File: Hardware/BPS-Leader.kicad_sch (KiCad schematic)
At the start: 27 parts, among them J17 Conn_01x04, J21 SFH11-PBPC-D05-ST-BK, J5 Conn_02x06_Counter_Clockwise, J6 PeripheralCAN, J7 PeripheralCAN, J8 CarCANConnector, Q11 PSMN8R5-40MSDX, U12 SHT4x

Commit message: revB updates
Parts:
- removed J17: Conn_01x04, UTSVT_Connectors:Molex_Nano-Fit_105309-xx04_1x04_P2.50mm_Vertical, symbol Connector_Generic:Conn_01x04
- removed J6: PeripheralCAN, UTSVT_Connectors:Molex_Nano-Fit_105309-xx04_1x04_P2.50mm_Vertical, symbol utsvt_connectors:PeripheralCANConnector
- removed LOGO2: UTSVT, UTSVT_Logos:LHRs_LOGO, symbol UTSVT_Misc:Logo_Placeholder
- removed LOGO3: Hallock, UTSVT_Logos:Hallock_Image_Small, symbol UTSVT_Misc:Logo_Placeholder
- removed Q11: PSMN8R5-40MSDX, UTSVT_Power:PSMN8R5-40MSDX, symbol Transistor_FET:BUK7M27-80EX
- added F3, F5: 3568, FUSE 3568:3568, symbol 3568:3568
- added J4: PeripheralCAN, UTSVT_Connectors:Molex_Nano-Fit_105309-xx04_1x04_P2.50mm_Vertical, symbol utsvt_connectors:PeripheralCANConnector
- added LOGO1, LOGO2, LOGO3, LOGO4: Dr. Hallock, symbol utsvt_misc:Logo_Placeholder
- added Q11: IRLML0030, Package_TO_SOT_SMD:SOT-23, symbol Transistor_FET:IRLML0030
- added R16, R17: 10k, Resistor_SMD:R_0603_1608Metric, symbol Device:R_US
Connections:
- net +24V: now also F3.2, F3.4, F5.2, F5.4; no longer J7.1 (24V)
- net +3.3V: now also R16.1, R17.1
- net ARRAY_PRE_CONTROL: now also J1.16 (SPI3_NSS); no longer J1.47 (ADC2_IN12)
- net CAR_CAN+: no longer J1.30 (CarCAN_H), J8.1 (CAN_H)
- net CAR_CAN-: no longer J1.32 (CarCAN_L), J8.2 (CAN_L)
- net ESP_RESET: now also J1.48 (SPI2_NSS); no longer J1.17 (UART5_TX)
- net FAN_ALERT: now also J1.47 (ADC2_IN12); no longer J1.31 (OPAMP5_VINM)
- net GND: now also J4.2 (GND), Q11.2 (S)
- net LED_RCLK: no longer J21.5 (CH5)
- net LED_SER: now also J1.20 (SPI3_SCK); no longer J1.16 (SPI3_NSS)
- net STROBE_CONN_24V-: now also Q11.3 (D)
- net STROBE_CONN_3.3V: now also Q11.1 (G)
- net BPS_CAN+ renamed BPS_CAN_H
- net BPS_CAN_H: now also J4.3 (CAN_H)
- net BPS_CAN- renamed BPS_CAN_L
- net BPS_CAN_L: now also J4.4 (CAN_L)
- net FAN+HTSense_SCL renamed HTSense_SCL
- net HTSense_SCL: now also J21.5 (CH5), R16.2; no longer J21.6 (CH4)
- net FAN+HTSense_SDA renamed HTSense_SDA
- net HTSense_SDA: now also J21.6 (CH4), R17.2; no longer J21.7 (CH3)
- net FAN_1_PWM renamed FAN_SDA
- net FAN_2_PWM renamed FAN_SCL
- net FAN_SCL: now also J21.7 (CH3)
- new net: F3.1, F3.3, J7.1 (24V)
- new net: F5.1, F5.3, J4.1 (24V)
- new net CAR_CAN_H: J1.30 (CarCAN_H), J8.1 (CAN_H)
- new net CAR_CAN_L: J1.32 (CarCAN_L), J8.2 (CAN_L)
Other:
- sheet Contactor Control and Sense ports: added ARRAY_PRE_VOLTAGE+_ADC, ARRAY_PRE_VOLTAGE-_ADC; removed none
- sheet Fan Controller ports: added none; removed FAN_1_PWM, FAN_2_PWM
- note added: "Icons"
- note removed: "(to be updated)"
- note removed: "Analog Input"
- note removed: "Load-bearing Icons"
- moved on the sheet: C36, J7, J8, TP2, TP3, U12

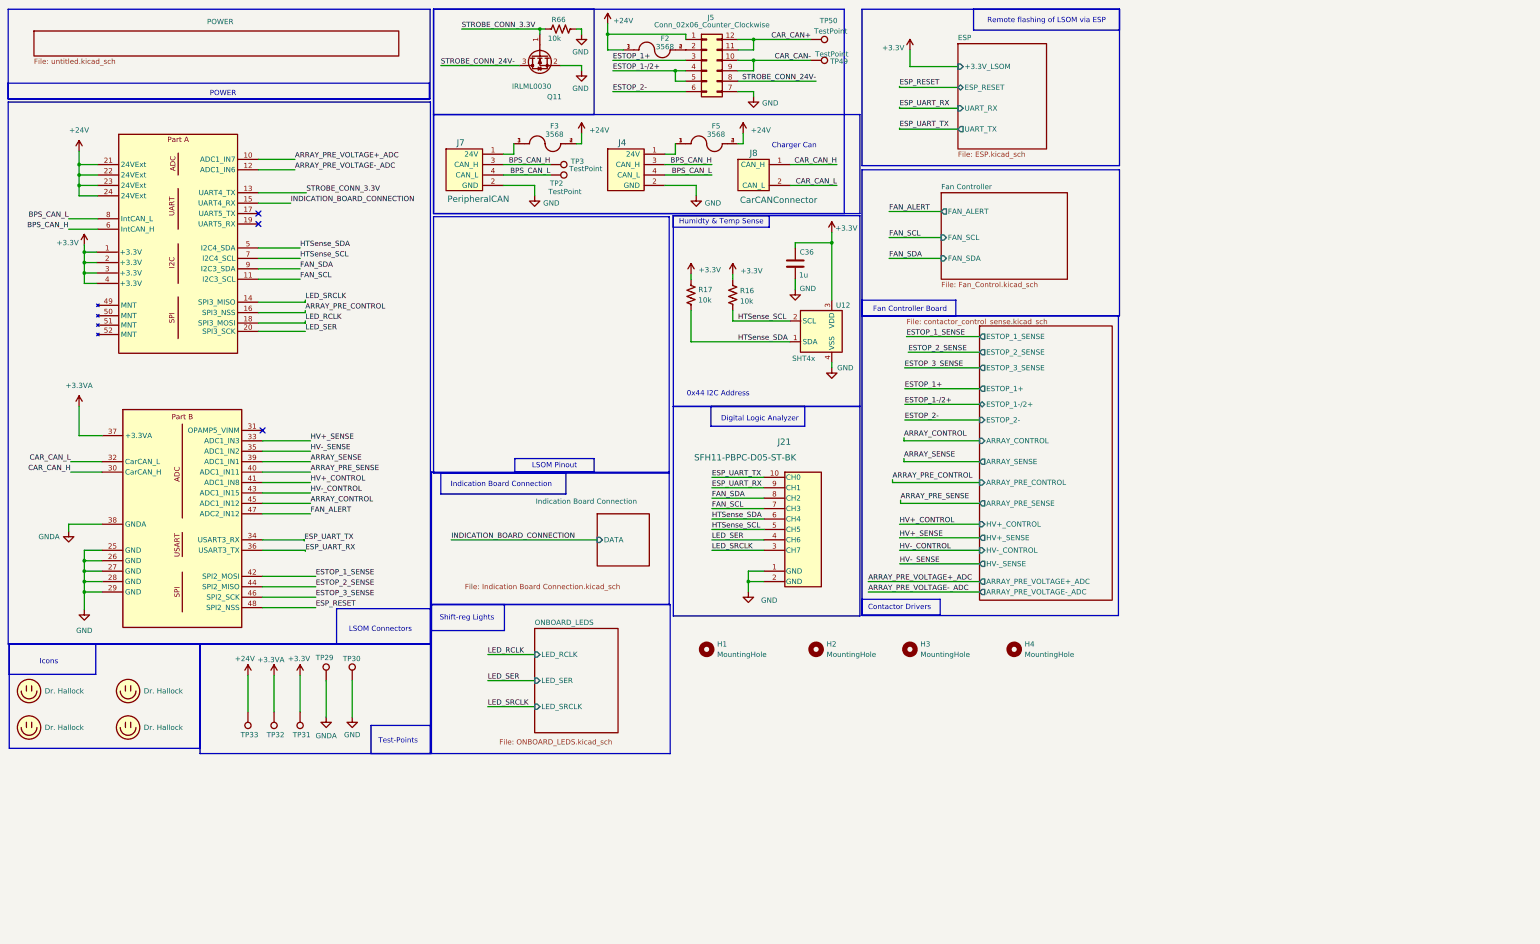
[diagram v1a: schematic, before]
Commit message: Schematic polishes, layout WIP
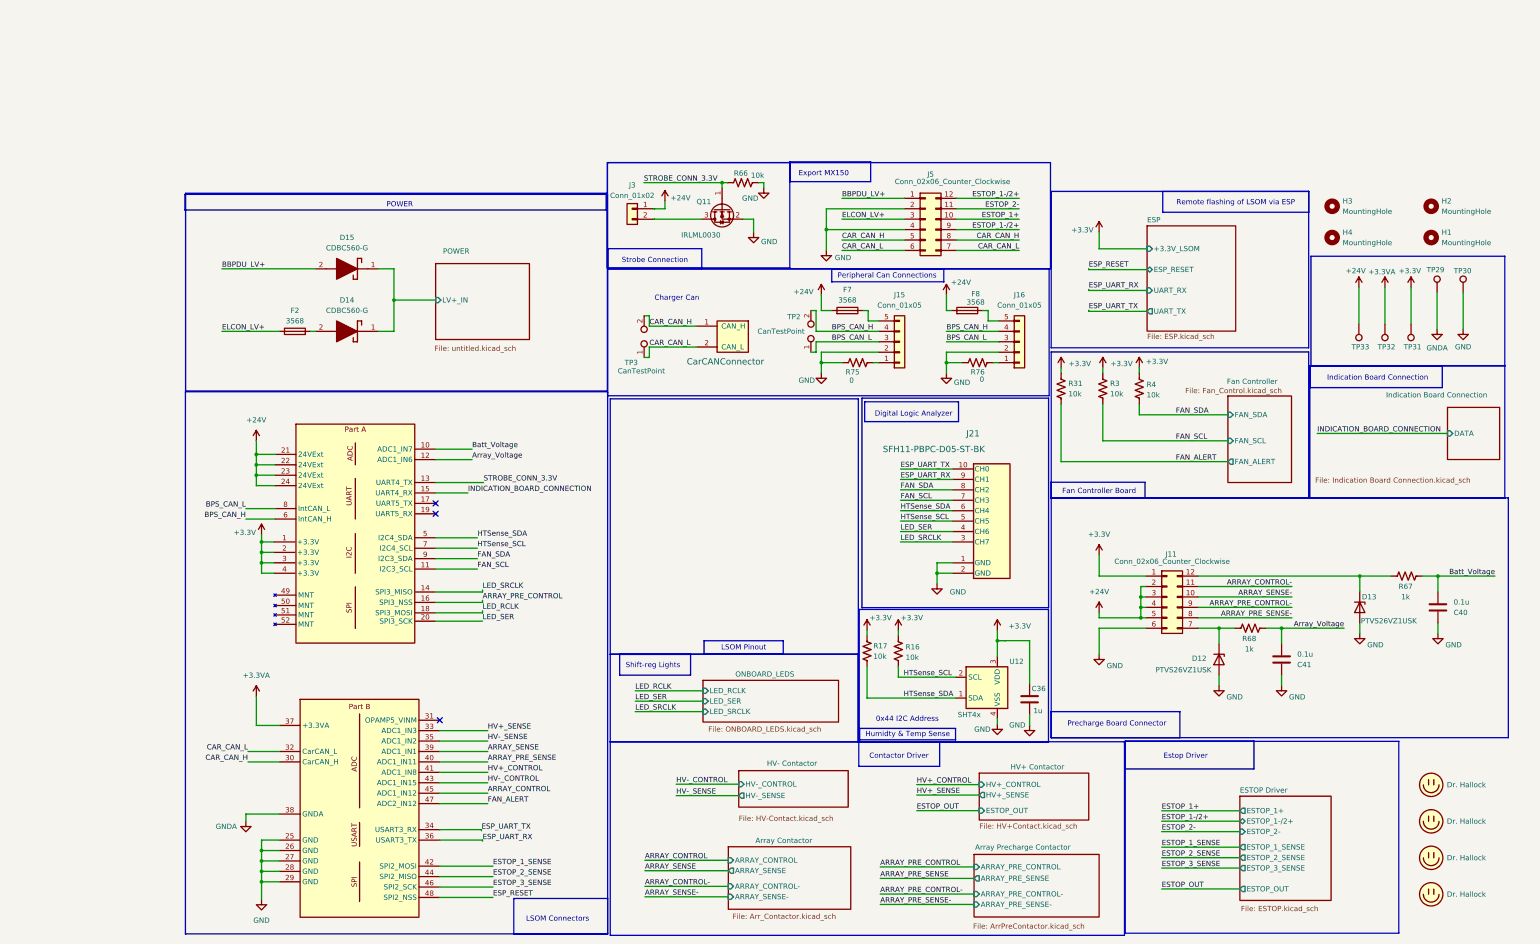
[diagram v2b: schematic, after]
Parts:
- removed F2, F3, F5: 3568, FUSE 3568:3568, symbol 3568:3568
- removed J4, J7: PeripheralCAN, UTSVT_Connectors:Molex_Nano-Fit_105309-xx04_1x04_P2.50mm_Vertical, symbol utsvt_connectors:PeripheralCANConnector
- removed TP2, TP3, TP49, TP50: TestPoint, TestPoint:TestPoint_Pad_1.0x1.0mm, symbol Connector:TestPoint
- added C40, C41: 0.1u, Capacitor_SMD:C_0603_1608Metric, symbol Device:C
- added D12, D13: PTVS26VZ1USK, Diode_SMD:Nexperia_DSN1608-2_1.6x0.8mm, symbol Diode:PTVS26VZ1USK
- added D14, D15: CDBC560-G, Schlotty:DIOM7959X262N, symbol CDBC560-G:CDBC560-G
- added F2, F7, F8: 3568, FUSE 3568:3568, symbol Device:Fuse
- added J11: Conn_02x06_Counter_Clockwise, Connector_Molex:Molex_Nano-Fit_105310-xx12_2x06_P2.50mm_Vertical, symbol Connector_Generic:Conn_02x06_Counter_Clockwise
- added J15, J16: Conn_01x05, Connector_Molex:Molex_Nano-Fit_105309-xx05_1x05_P2.50mm_Vertical, symbol Connector_Generic:Conn_01x05
- added J3: Conn_01x02, Connector_Molex:Molex_Nano-Fit_105313-xx02_1x02_P2.50mm_Horizontal, symbol Connector_Generic:Conn_01x02
- added R3, R31, R4: 10k, Resistor_SMD:R_0603_1608Metric, symbol Device:R_US
- added R67, R68: 1k, Resistor_SMD:R_0603_1608Metric, symbol Device:R_US
- added R75, R76: 0, Resistor_SMD:R_0603_1608Metric, symbol Device:R_US
- added TP2, TP3: CanTestPoint, Connector_PinHeader_2.54mm:PinHeader_1x02_P2.54mm_Vertical, symbol Connector:TestPoint_2Pole
- J5: footprint Connector_Molex:Molex_Nano-Fit_105310-xx12_2x06_P2.50mm_Vertical -> UTSVT_Connectors:MX150_02x06_Vertical
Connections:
- net +24V: now also F7.2, F8.2, J11.2 (Pin_2), J11.3 (Pin_3), J11.4 (Pin_4), J11.5 (Pin_5), J3.1 (Pin_1); no longer J5.1 (Pin_1)
- net +3.3V: now also J11.1 (Pin_1), R3.1, R31.1, R4.1
- net BPS_CAN_H: now also J15.4 (Pin_4), J16.4 (Pin_4), TP2.2
- net BPS_CAN_L: now also J15.3 (Pin_3), J16.3 (Pin_3), TP2.1
- net CAR_CAN_H: now also J5.5 (Pin_5), J5.8 (Pin_8), TP3.2
- net CAR_CAN_L: now also J5.6 (Pin_6), J5.7 (Pin_7), TP3.1
- net ESTOP_1+: now also J5.10 (Pin_10); no longer J5.3 (Pin_3)
- net ESTOP_1-/2+: now also J5.12 (Pin_12), J5.9 (Pin_9); no longer J5.4 (Pin_4), J5.5 (Pin_5)
- net ESTOP_2-: now also J5.11 (Pin_11); no longer J5.6 (Pin_6)
- net FAN_ALERT: now also R31.2
- net FAN_SCL: now also R3.2
- net FAN_SDA: now also R4.2
- net GND: now also J5.2 (Pin_2), J5.4 (Pin_4), C40.1, C41.1, D12.2 (A), D13.2 (A), J11.6 (Pin_6), J15.2 (Pin_2), J16.2 (Pin_2), R75.1, R76.1; no longer J5.7 (Pin_7)
- net ARRAY_PRE_VOLTAGE+_ADC renamed Batt_Voltage
- net Batt_Voltage: now also C40.2, R67.1
- net ARRAY_PRE_VOLTAGE-_ADC renamed Array_Voltage
- net Array_Voltage: now also C41.2, R68.1
- removed net CAR_CAN+: J5.11 (Pin_11), J5.12 (Pin_12)
- removed net CAR_CAN-: J5.10 (Pin_10), J5.9 (Pin_9)
- net STROBE_CONN_24V-: no longer names the net of Q11.3 (D)
- net STROBE_CONN_24V-: now also J3.2 (Pin_2); no longer J5.8 (Pin_8)
- new net: D13.1 (K), J11.12 (Pin_12), R67.2
- new net: J16.1 (Pin_1), R76.2
- new net: F8.1, J16.5 (Pin_5)
- new net: J15.1 (Pin_1), R75.2
- new net: F7.1, J15.5 (Pin_5)
- new net: D12.1 (K), J11.7 (Pin_7), R68.2
- new net: D14.2 (A), F2.2
- new net ARRAY_CONTROL-: J11.11 (Pin_11)
- new net ARRAY_PRE_CONTROL-: J11.9 (Pin_9)
- new net ARRAY_PRE_SENSE-: J11.8 (Pin_8)
- new net ARRAY_SENSE-: J11.10 (Pin_10)
- new net BBPDU_LV+: D15.2 (A), J5.1 (Pin_1)
- new net ELCON_LV+: F2.1, J5.3 (Pin_3)
- new net POWER/LV+_IN: D14.1 (K), D15.1 (K)
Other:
- removed sheet Contactor Control and Sense
- added sheet Array Contactor (Arr_Contactor.kicad_sch)
- added sheet Array Precharge Contactor (ArrPreContactor.kicad_sch)
- added sheet ESTOP Driver (ESTOP.kicad_sch)
- added sheet HV+ Contactor (HV+Contact.kicad_sch)
- added sheet HV- Contactor (HV-Contact.kicad_sch)
- sheet POWER ports: added LV+_IN; removed none
- note added: "Contactor Driver"
- note added: "Estop Driver"
- note added: "Export MX150"
- note added: "Peripheral Can Connections"
- note added: "Precharge Board Connector"
- note added: "Strobe Connection"
- note removed: "Contactor Drivers"
- note removed: "Icons"
- note removed: "Test-Points"
- moved on the sheet: C36, H1, H2, H3, H4, J21, Q11, R16, R17, R66, TP29, TP30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

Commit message: circuit blocks designed, schematic updated
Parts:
- removed D14: CDBC560-G, Schlotty:DIOM7959X262N, symbol CDBC560-G:CDBC560-G
- removed F7, F8: 3568, FUSE 3568:3568, symbol Device:Fuse
- removed TP29, TP32: TestPoint, TestPoint:TestPoint_Pad_1.0x1.0mm, symbol Connector:TestPoint
- added F3: 3568, FUSE 3568:3568, symbol Device:Fuse
- J5: footprint UTSVT_Connectors:MX150_02x06_Vertical -> Connector_Molex:Molex_Nano-Fit_105310-xx12_2x06_P2.50mm_Vertical
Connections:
- net POWER/LV+_IN is gone; now on net +24V: D15.1 (K)
- net +24V: now also F3.2
- net BBPDU_LV+: now also F2.2; no longer D15.2 (A)
- net FUSED_24V: now reaches J16.5 (Pin_5)
- net FUSED_24V: now also J15.5 (Pin_5), F3.1
- new net POWER/LV_OUT: D15.2 (A)
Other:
- sheet POWER ports: added LV_OUT; removed none
- moved on the sheet: D15, F2

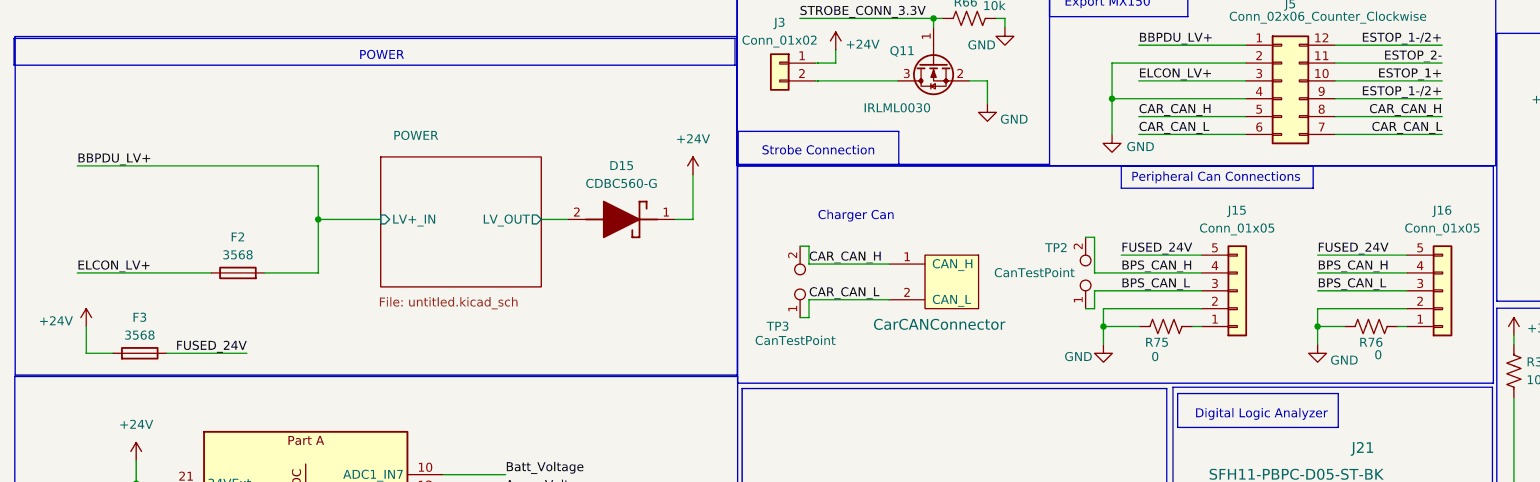
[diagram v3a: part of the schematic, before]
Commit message: small schematic changes
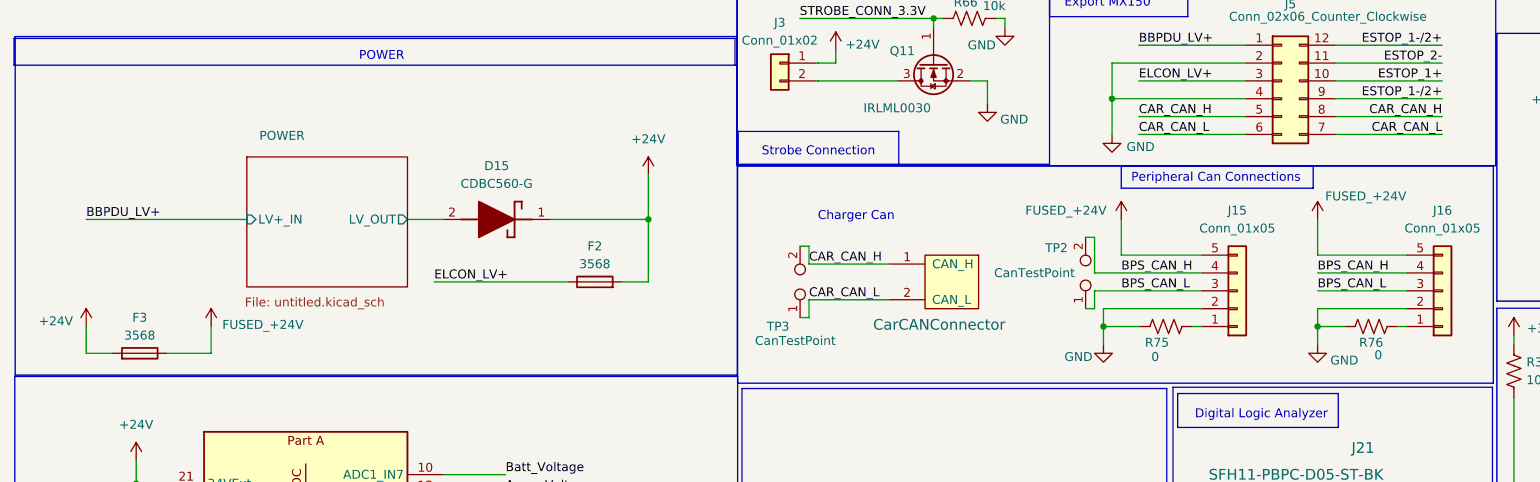
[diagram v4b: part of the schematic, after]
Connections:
- net +24V: now also F2.2
- net BBPDU_LV+: no longer F2.2
- net FUSED_24V renamed FUSED_+24V
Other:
- moved on the sheet: D15, F2

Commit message: intial layout design
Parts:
- removed D12, D13: PTVS26VZ1USK, Diode_SMD:Nexperia_DSN1608-2_1.6x0.8mm, symbol Diode:PTVS26VZ1USK
- removed D15: CDBC560-G, Schlotty:DIOM7959X262N, symbol CDBC560-G:CDBC560-G
- added D12, D13: TVS, Diode_SMD:D_SOD-123F, symbol Device:D_Zener
- added TP1, TP5: TestPoint, TestPoint:TestPoint_Pad_1.0x1.0mm, symbol Connector:TestPoint
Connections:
- net +3.3V: no longer J11.1 (Pin_1)
- net +3.3VA: now also J11.1 (Pin_1), TP1.1
- net ARRAY_PRE_SENSE: now also J1.48 (SPI2_NSS); no longer J1.40 (ADC1_IN11)
- net ESP_RESET: now also J1.40 (ADC1_IN11); no longer J1.48 (SPI2_NSS)
- net ESTOP_1_SENSE: now also J1.46 (SPI2_SCK); no longer J1.42 (SPI2_MOSI)
- net ESTOP_3_SENSE: now also J1.42 (SPI2_MOSI); no longer J1.46 (SPI2_SCK)
- net GND: no longer C40.1, C41.1
- net GNDA: now also C40.1, C41.1, D12.2 (A), D13.2 (A), TP5.1
- net at J11.12 (Pin_12), R67.2: now also D13.1 (K)
- net at J11.7 (Pin_7), R68.2: now also D12.1 (K)
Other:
- moved on the sheet: C40, R67

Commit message: RevB layout completed
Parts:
- removed H1, H2, H3, H4: MountingHole, MountingHole:MountingHole_3.2mm_M3, symbol Mechanical:MountingHole
- added H1, H2, H3, H4: MountingHole_Pad, MountingHole:MountingHole_3.2mm_M3_Pad_TopBottom, symbol Mechanical:MountingHole_Pad
- LOGO1: value Dr. Hallock -> LHRs; footprint (none) -> UTSVT_Logos:LHRs_LOGO
- LOGO2: footprint (none) -> UTSVT_Logos:Hallock_Image
- LOGO3: value Dr. Hallock -> Beach; footprint (none) -> Custom-KiCadLibraries:Beach
- LOGO4: value Dr. Hallock -> Gear; footprint (none) -> Custom-KiCadLibraries:Gear
- TP1: value TestPoint -> +3.3VA; footprint TestPoint:TestPoint_Pad_1.0x1.0mm -> TestPoint:TestPoint_Keystone_5005-5009_Compact
- TP30: value TestPoint -> GND; footprint TestPoint:TestPoint_Pad_1.0x1.0mm -> TestPoint:TestPoint_Keystone_5005-5009_Compact
- TP31: value TestPoint -> +3.3V; footprint TestPoint:TestPoint_Pad_1.0x1.0mm -> TestPoint:TestPoint_Keystone_5005-5009_Compact
- TP33: value TestPoint -> +24V; footprint TestPoint:TestPoint_Pad_1.0x1.0mm -> TestPoint:TestPoint_Keystone_5005-5009_Compact
- TP5: value TestPoint -> GNDA; footprint TestPoint:TestPoint_Pad_1.0x1.0mm -> TestPoint:TestPoint_Keystone_5005-5009_Compact
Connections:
- no-connect marks 3 -> 7

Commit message: JLC Production Files
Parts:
- C36: LCSC (none) -> C15849
- C40, C41: LCSC (none) -> C14663
- D12, D13: LCSC (none) -> C283866
- F2, F3: LCSC (none) -> C5249699
- Q11: LCSC (none) -> C67272
- R16, R17, R3, R31, R4, R66: LCSC (none) -> C25804
- R67, R68: LCSC (none) -> C21190
- R75, R76: LCSC (none) -> C21189
- U12: LCSC (none) -> C5221601
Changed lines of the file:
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@@
 			)
 		)
+		(property "LCSC" "C25804"
+			(at 224.7518 171.8928 0)
+			(effects
+				(font
+					(size 1.27 1.27)
+				)
+				(hide yes)
+			)
+		)
 		(pin "1"
 		)
@@
 			)
 		)
+		(property "LCSC" "C21189"
+			(at 219.71 105.156 0)
+			(effects
+				(font
+					(size 1.27 1.27)
+				)
+				(hide yes)
+			)
+		)
 		(pin "2"
 		)
@@
 			)
 		)
+		(property "LCSC" "C67272"
+			(at 185.2478 63.6559 0)
+			(effects
+				(font
+					(size 1.27 1.27)
+				)
+				(hide yes)
+			)
+		)
 		(pin "1"
 		)
@@
 			)
 		)
+		(property "LCSC" "C283866"
+			(at 346.075 161.2899 0)
+			(effects
+				(font
+					(size 1.27 1.27)
+				)
+				(hide yes)
+			)
+		)
 		(pin "2"
 		)
@@
 			)
 		)
+		(property "LCSC" "C283866"
+			(at 304.038 173.99 0)
+			(effects
+				(font
+					(size 1.27 1.27)
+				)
+				(hide yes)
+			)
+		)
 		(pin "2"
 		)
@@
 			)
 		)
+		(property "LCSC" "C5249699"
+			(at 74.93 101.6 0)
+			(effects
+				(font
+					(size 1.27 1.27)
+				)
+				(hide yes)
+			)
+		)
 		(pin "1"
 		)
@@
 			)
 		)
+		(property "LCSC" "C25804"
+			(at 282.448 107.9499 0)
+			(effects
+				(font
+					(size 1.27 1.27)
+				)
+				(hide yes)
+			)
+		)
 		(pin "1"
 		)
@@
 			)
 		)
+		(property "LCSC" "C21190"
+			(at 316.3503 170.1156 0)
+			(effects
+				(font
+					(size 1.27 1.27)
+				)
+				(hide yes)
+			)
+		)
 		(pin "2"
 		)
@@
 			)
 		)
+		(property "LCSC" "C25804"
+			(at 291.338 108.2039 0)
+			(effects
+				(font
+					(size 1.27 1.27)
+				)
+				(hide yes)
+			)
+		)
 		(pin "1"
 		)
@@
 			)
 		)
+		(property "LCSC" "C5249699"
+			(at 139.7 91.44 0)
+			(effects
+				(font
+					(size 1.27 1.27)
+				)
+				(hide yes)
+			)
+		)
 		(pin "1"
 		)
@@
 			)
 		)
+		(property "LCSC" "C21190"
+			(at 351.79 149.86 0)
+			(effects
+				(font
+					(size 1.27 1.27)
+				)
+				(hide yes)
+			)
+		)
 		(pin "2"
 		)
@@
 			)
 		)
+		(property "LCSC" "C5221601"
+			(at 257.9106 175.6877 0)
+			(effects
+				(font
+					(size 1.27 1.27)
+				)
+				(hide yes)
+			)
+		)
 		(pin "4"
 		)
@@
 			)
 		)
+		(property "LCSC" "C25804"
+			(at 232.6258 172.1467 0)
+			(effects
+				(font
+					(size 1.27 1.27)
+				)
+				(hide yes)
+			)
+		)
 		(pin "1"
 		)
@@
 			)
 		)
+		(property "LCSC" "C25804"
+			(at 272.288 107.9499 0)
+			(effects
+				(font
+					(size 1.27 1.27)
+				)
+				(hide yes)
+			)
+		)
 		(pin "1"
 		)
@@
 			)
 		)
+		(property "LCSC" "C14663"
+			(at 361.95 163.8301 0)
+			(effects
+				(font
+					(size 1.27 1.27)
+				)
+				(hide yes)
+			)
+		)
 		(pin "1"
 		)
@@
 			)
 		)
+		(property "LCSC" "C21189"
+			(at 250.19 105.156 0)
+			(effects
+				(font
+					(size 1.27 1.27)
+				)
+				(hide yes)
+			)
+		)
 		(pin "2"
 		)
@@
 			)
 		)
+		(property "LCSC" "C25804"
+			(at 192.4801 56.7335 0)
+			(effects
+				(font
+					(size 1.27 1.27)
+				)
+				(hide yes)
+			)
+		)
 		(pin "2"
 		)
@@
 			)
 		)
+		(property "LCSC" "C14663"
+			(at 328.0343 176.4657 0)
+			(effects
+				(font
+					(size 1.27 1.27)
+				)
+				(hide yes)
+			)
+		)
 		(pin "1"
 		)
@@
 			(effects
 				(font
+					(size 1.27 1.27)
+				)
+				(hide yes)
+			)
+		)
+		(property "LCSC" "C15849"
+			(at 265.0423 182.3076 0)
+			(effects
+				(font
